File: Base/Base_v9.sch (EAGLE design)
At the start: 17 parts, among them IC1 74HC595, IC2 74HC595, IC3 K155ID, IC4 K155ID, IC5 K155ID, IC6 K155ID, J1 694106301002, J2 694106301002, K1 ZNS5106, Q1 PNP

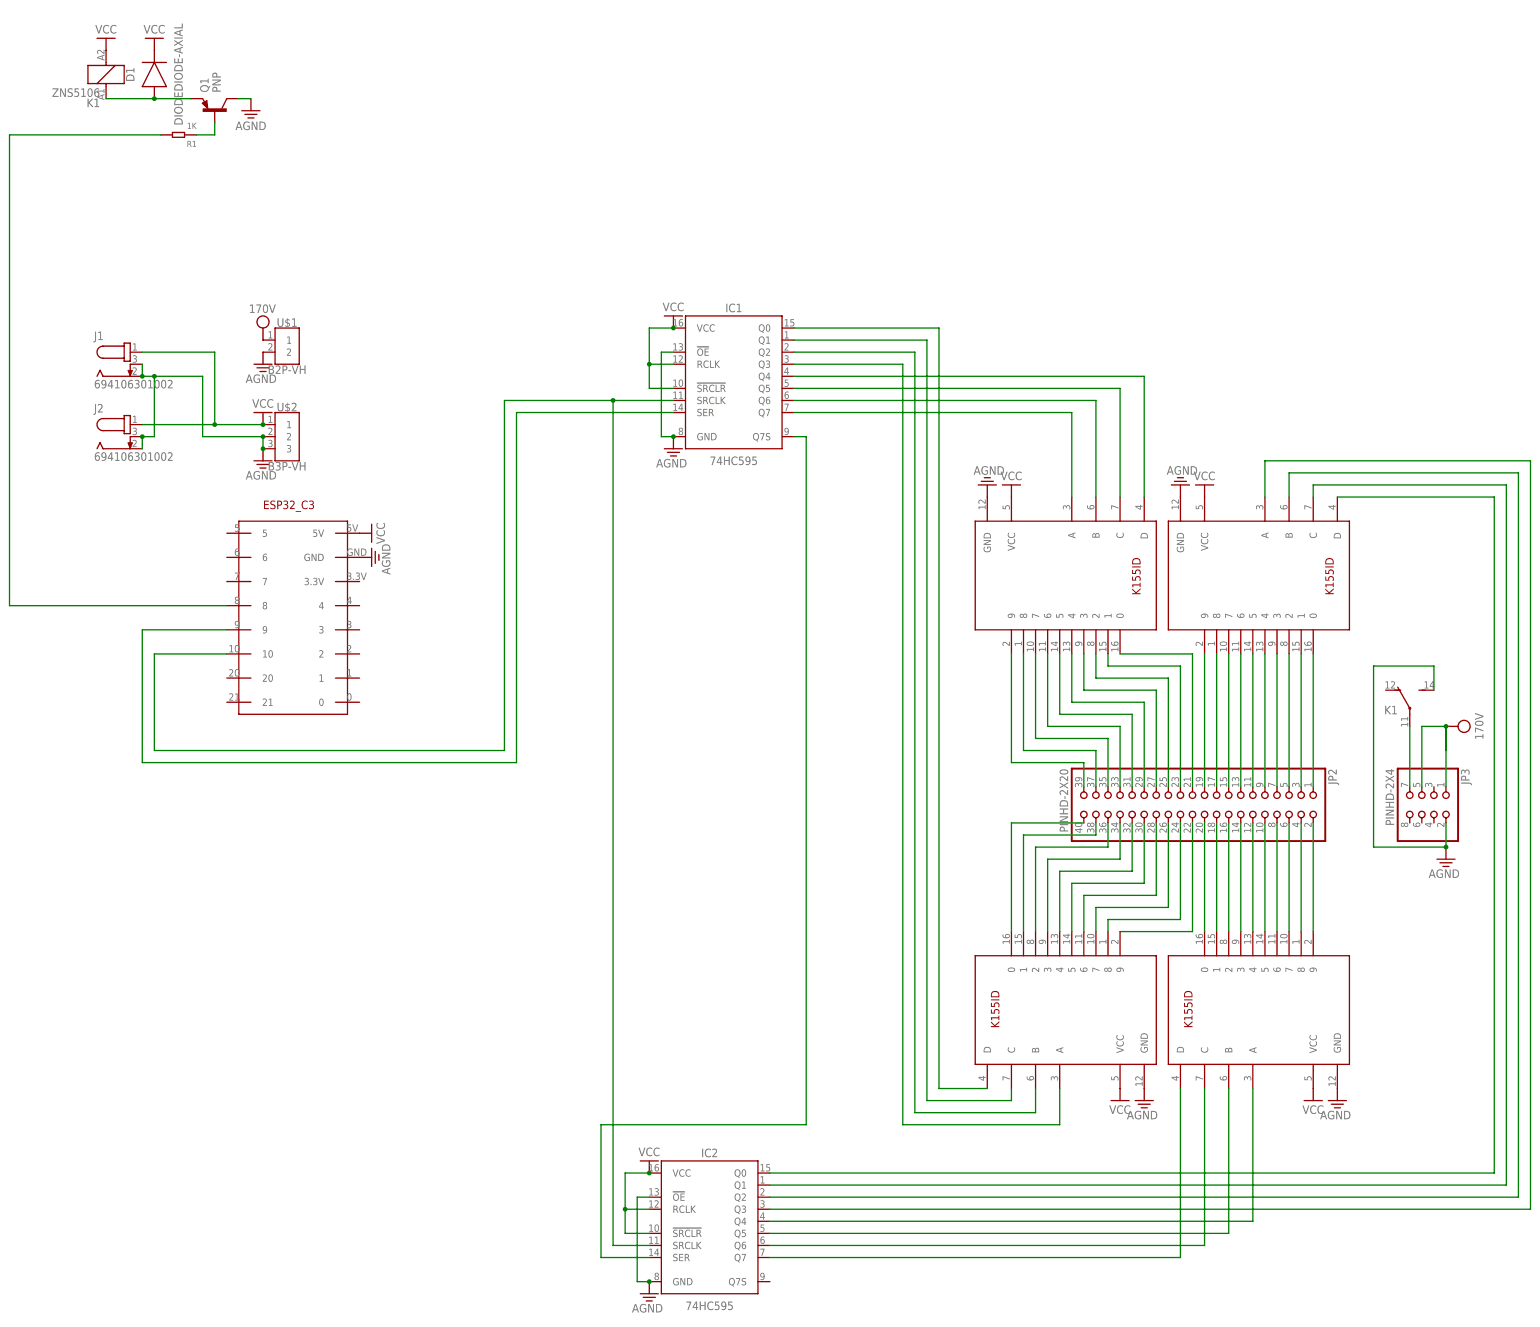
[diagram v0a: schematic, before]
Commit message: Fixed shift register clock lines
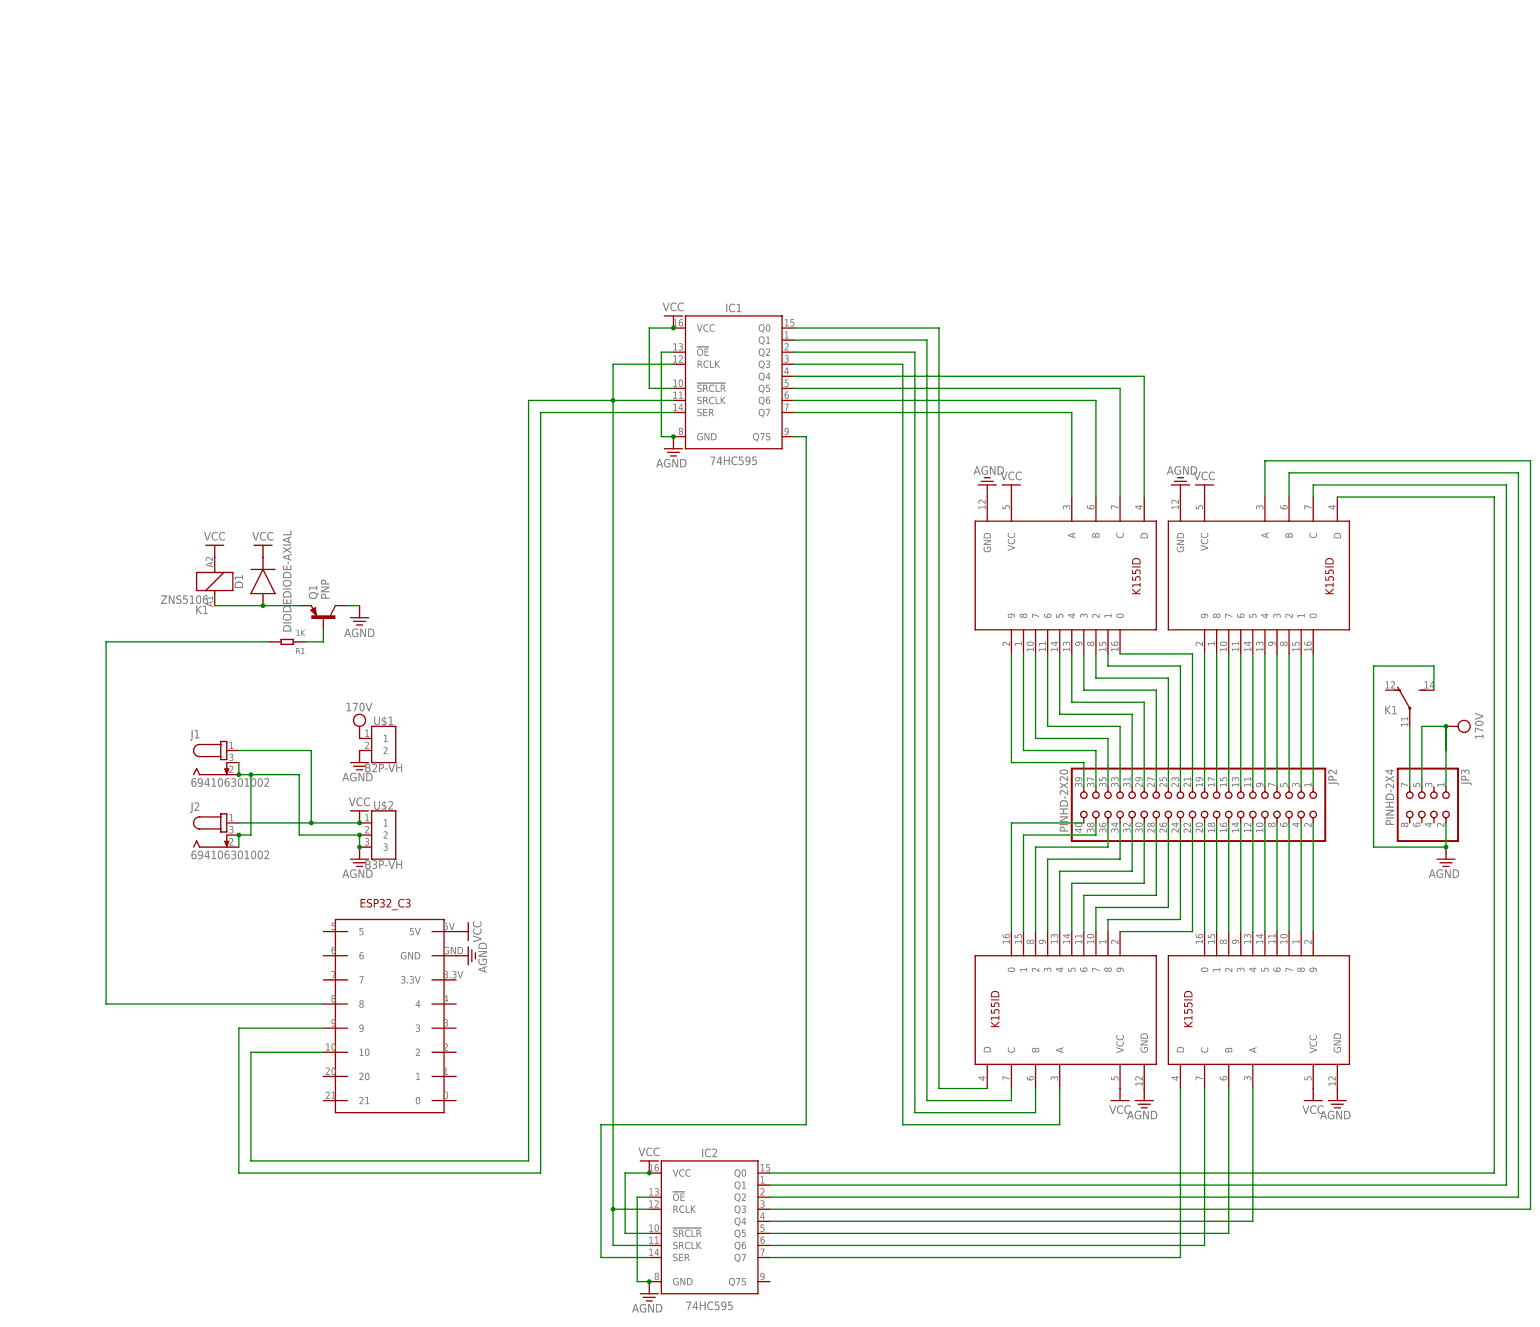
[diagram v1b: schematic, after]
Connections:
- net N$58: now also IC1.RCLK, IC2.RCLK
- net VCC: no longer IC1.RCLK, IC2.RCLK
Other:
- moved on the sheet: D1, J1, J2, K1, Q1, R1, U$1, U$2
